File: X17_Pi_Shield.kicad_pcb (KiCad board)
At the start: 4 copper layers, 85 x 56 mm, 89 parts, among them J1 BM04B-GHS-TBT, J10 BM04B-GHS-TBT, J11 BM04B-GHS-TBT, J12 Conn_01x05_Pin, J13 Conn_01x03_Pin, J2 BM02B-GHS-TBT, J20 Conn_01x02_Pin, J22 430450212, J23 430450612, J24 430450212, J3 BM02B-GHS-TBT, J4 BM02B-GHS-TBT, J5 BM02B-GHS-TBT, J6 Conn_01x03_Pin, J7 BM04B-GHS-TBT, J8 UJC-HP-L-G-5-MSMT-TR, J9 Conn_01x03_Pin, U1 4754, U10 4754, U2 TPS2117DRLR, U3 INA260AIPW, U5 MAX485, U6 MMBT3906LT3G, U7 ISOW1432BDFMR, U8 RASPBERRY_PI_4B_4GB, U9 AZ1117IH-3.3TRG1

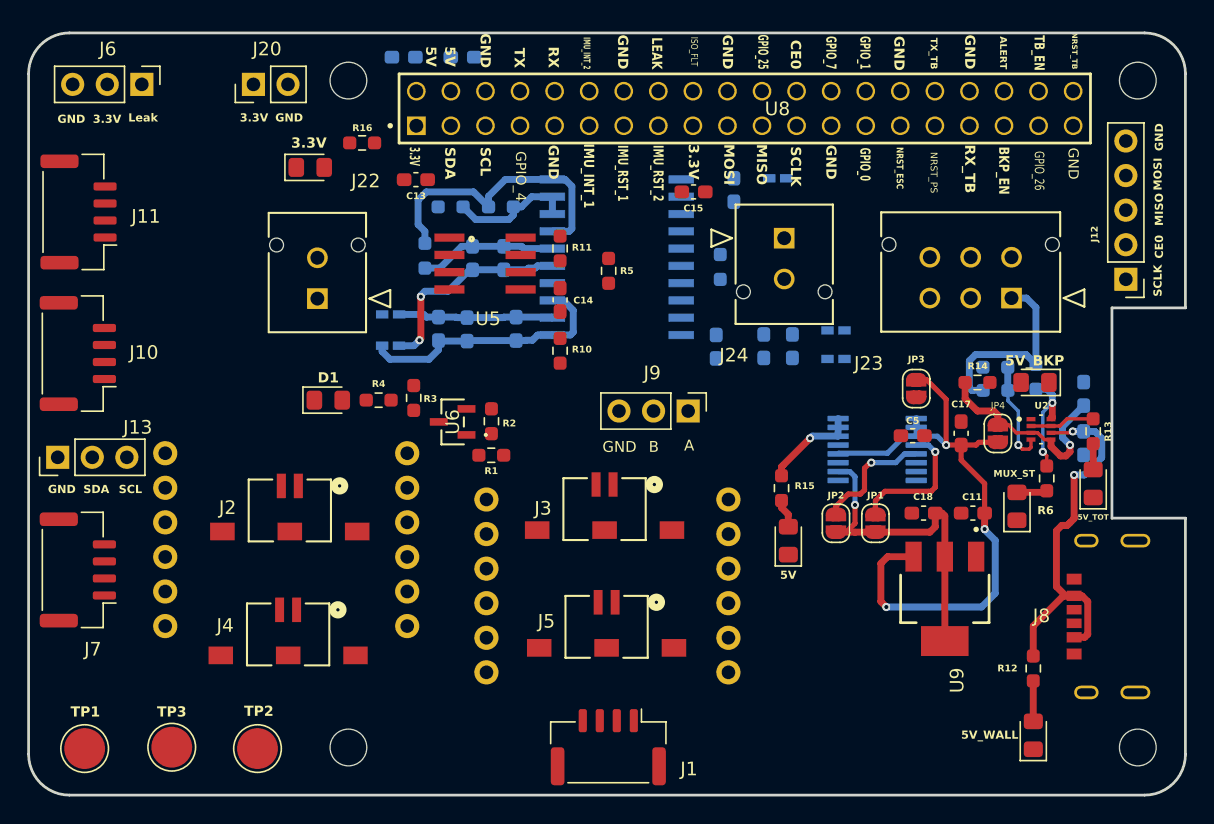
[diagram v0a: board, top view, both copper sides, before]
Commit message: Routing Additions
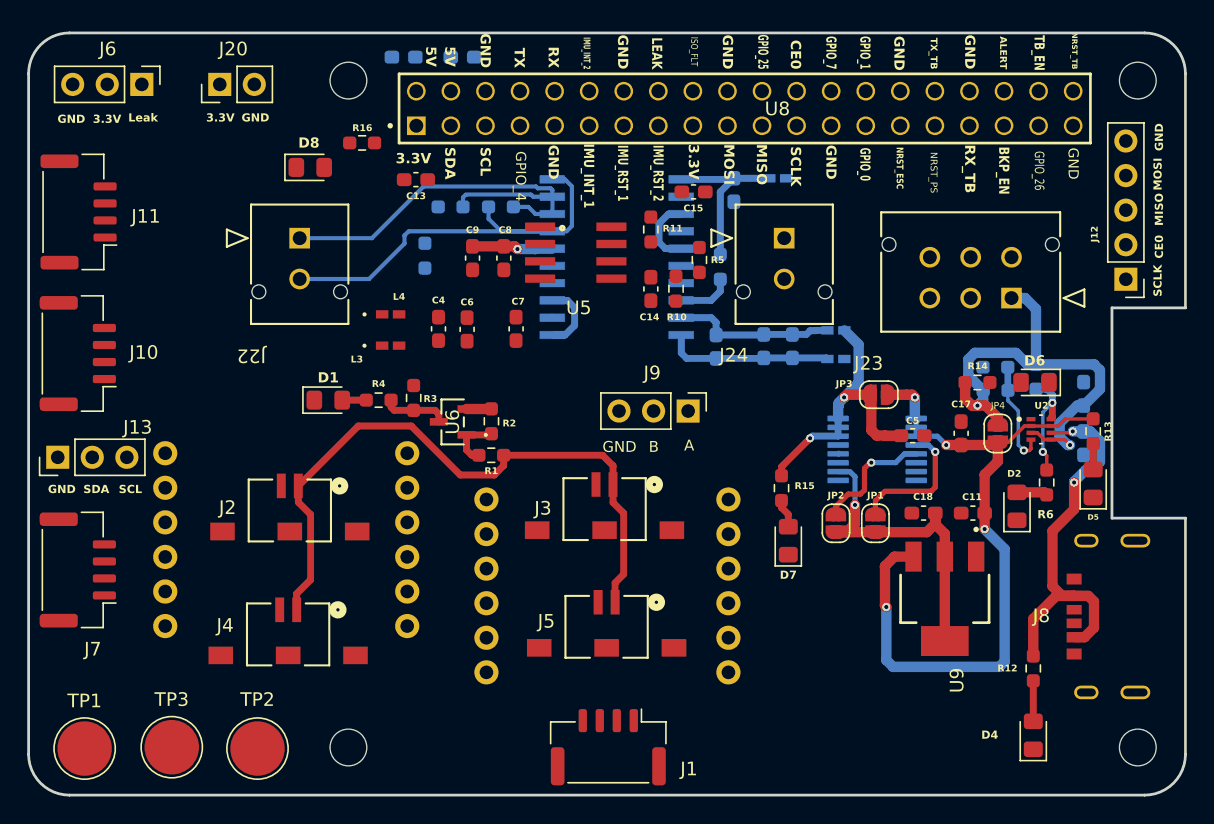
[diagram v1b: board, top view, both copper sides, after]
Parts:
- C4, C6, C7, C8, C9, L3, L4: moved to F.Cu
- TP1, TP2, TP3: footprint TestPoint:TestPoint_Pad_D3.0mm -> TestPoint:TestPoint_Pad_D4.0mm
- moved R10 9.66 mm to (157.2, 97.0)
- moved R11 6.81 mm to (155.4, 92.7)
- moved U5 6.72 mm to (149.9, 94.4)
- moved C14 6.72 mm to (155.4, 97.0)
- moved R5 6.72 mm to (159.0, 94.9)
- moved J22 4.63 mm to (129.6, 93.3), turned to 180 degrees
- moved JP3 2.79 mm to (172.2, 104.8), turned to 180 degrees
- moved J20 2.48 mm to (123.7, 82.0)
- moved R6 0.30 mm to (184.5, 111.2)
- renumbered MUX_ST to D2, 5V_WALL to D4, 5V_TOT to D5, 5V_BKP to D6, 5V to D7, 3.3V to D8
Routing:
- net /Sensors/PROBE: track 0.00 -> 48.3 mm
- net Net-(U7-B): track 9.26 -> 32.5 mm
- net GND_TB: track 15.6 -> 0.18 mm, vias 2 -> 0
- net +5V: track 7.04 -> 21.5 mm, vias 1 -> 2
- net Net-(U7-GND2): track 19.4 -> 5.09 mm
- net Net-(U7-VIO): track 0.00 -> 12.5 mm
- net Net-(U7-GND1): track 0.00 -> 12.3 mm
- net Net-(U7-VDD): track 0.00 -> 11.9 mm
- net Net-(U7-VISOOUT): track 11.4 -> 0.06 mm
- net Net-(U7-A): track 21.5 -> 32.5 mm
- net /Power/5V_BACKPLANE: track 30.4 -> 36.0 mm, vias 1 -> 2
- net /Pi + IMU/TB_EN: track 0.00 -> 5.13 mm
- net /Pi + IMU/LEAK: track 0.00 -> 4.81 mm
- net +3V3_TB: track 10.1 -> 5.95 mm, vias 0 -> 1
- net Net-(U6-BASE): track 0.00 -> 4.05 mm
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- added copper zone on In2.Cu, net +3V3
- added copper zone on In1.Cu, net GND

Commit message: Finished Routing
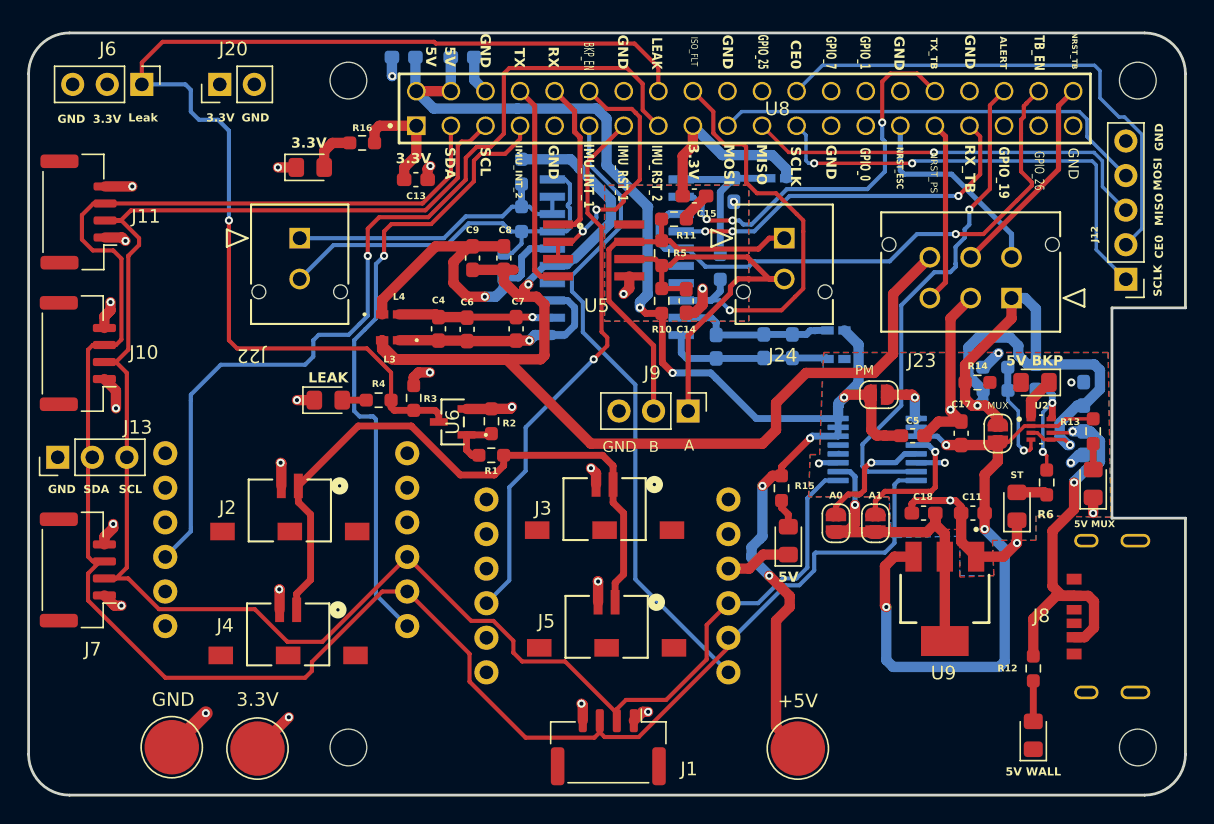
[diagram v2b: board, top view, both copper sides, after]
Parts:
- 5V BKP: renamed from D6
- 5V MUX: renamed from D5
- 5V WALL: renamed from D4
- moved +5V 52.4 mm to (166.2, 130.8)
- moved R20 5.85 mm to (144.6, 95.3)
- moved R19 5.82 mm to (145.9, 88.4), turned to 90 degrees
- moved R5 2.81 mm to (156.2, 94.4)
- moved C14 2.74 mm to (158.0, 97.9)
- moved R11 1.86 mm to (157.1, 91.9), turned to 0 degrees
- moved R17 1.76 mm to (145.9, 91.9), turned to -90 degrees
- moved R10 1.38 mm to (156.2, 97.9)
- moved U5 1.33 mm to (151.2, 94.2)
- moved L3 0.40 mm to (136.3, 100.8), turned to 180 degrees
- moved C15 0.31 mm to (158.6, 90.2)
- renumbered TP1 to +5V, D8 to 3.3V, TP2 to 3.3V, D7 to 5V, JP2 to A0, JP1 to A1, TP3 to GND, D1 to LEAK, JP4 to MUX, JP3 to PM, D2 to ST
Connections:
- U8 pad 07: (no net) -> /Pi + IMU/IMU_INT_2
- U8 pad 12: /Pi + IMU/IMU_INT_2 -> /Pi + IMU/BKP_EN
- U8 pad 35: /Pi + IMU/BKP_EN -> unconnected-(U8-GPIO19-Pad35)
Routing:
- net /Pi + IMU/SDA: track 0.00 -> 151.1 mm
- net /Pi + IMU/SCL: track 0.00 -> 139.9 mm
- net GND_TB: track 0.18 -> 96.1 mm, vias 0 -> 1
- net /Pi + IMU/LEAK: track 4.81 -> 86.6 mm, vias 0 -> 1
- net +5V: track 21.5 -> 102.9 mm, vias 2 -> 6
- net GND: track 0.00 -> 75.6 mm, vias 0 -> 26
- net /Pi + IMU/IMU_RST_2: track 0.00 -> 67.9 mm, vias 0 -> 1
- net /Pi + IMU/IMU_INT_1: track 0.00 -> 47.4 mm
- net /Pi + IMU/IMU_INT_2: track 0.00 -> 46.8 mm, vias 0 -> 1
- net /Pi + IMU/IMU_RST_1: track 0.00 -> 40.5 mm, vias 0 -> 1
- net /Pi + IMU/CE0: track 0.00 -> 38.0 mm
- net /Pi + IMU/ALERT: track 0.00 -> 36.7 mm, vias 0 -> 1
- net /Pi + IMU/TB_EN: track 5.13 -> 41.7 mm, vias 0 -> 1
- net +3V3: track 1.84 -> 36.4 mm, vias 0 -> 6
- net /Pi + IMU/SCLK: track 0.00 -> 33.8 mm, vias 0 -> 2
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- added copper zone on B.Cu, net GND
- added copper zone on F.Cu, net GND
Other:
- board text added: "GPIO_19"
- board text removed: "GPIO_4"

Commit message: Finished Layout + Updated Capacitor Sizes for 150uF
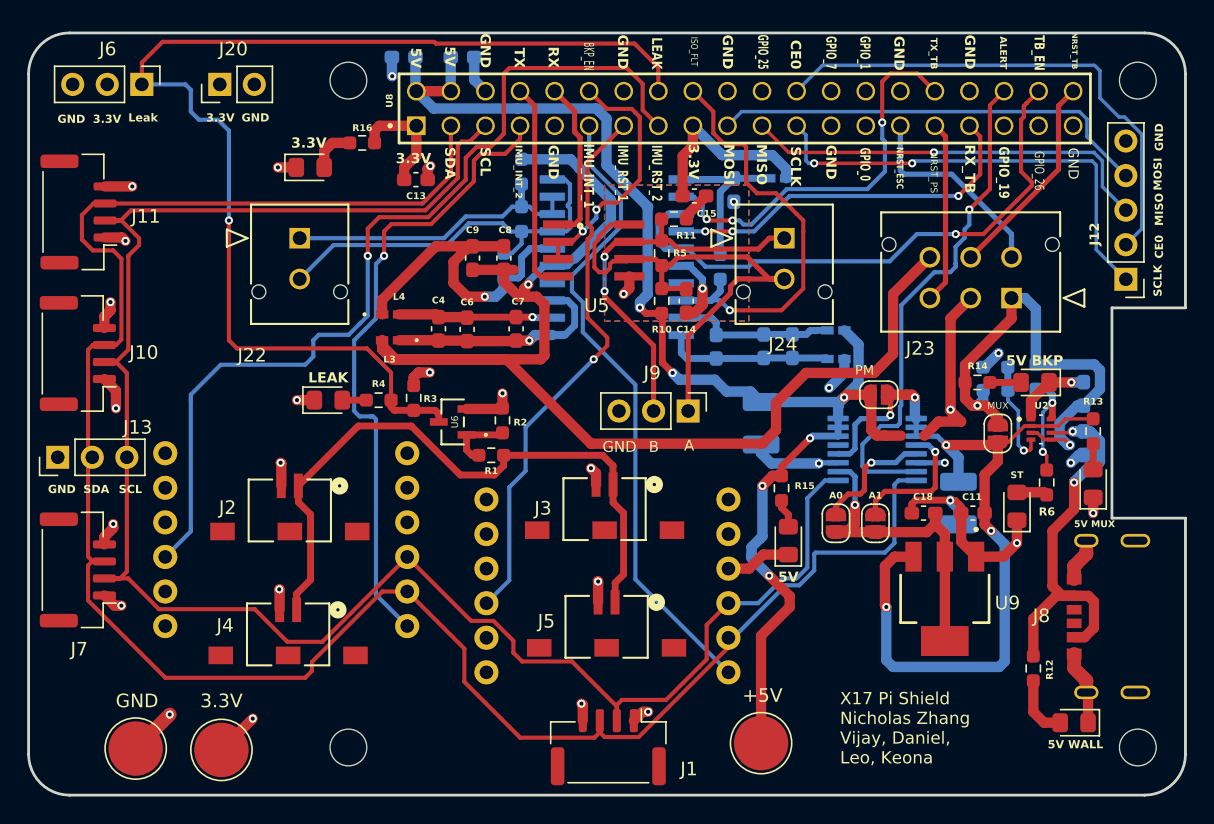
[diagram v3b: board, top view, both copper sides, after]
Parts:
- C17, C5: footprint Capacitor_SMD:C_0603_1608Metric_Pad1.08x0.95mm_HandSolder -> Capacitor_SMD:C_1210_3225Metric_Pad1.33x2.70mm_HandSolder; moved to B.Cu
- moved C5 11.2 mm to (163.5, 106.9), turned to -90 degrees
- moved C17 5.13 mm to (178.0, 112.8), turned to -90 degrees
- moved 5V WALL 3.14 mm to (186.5, 128.9), turned to 180 degrees
- moved +5V 2.73 mm to (163.5, 130.4)
- moved GND 2.65 mm to (117.5, 130.8)
- moved 3.3V 2.65 mm to (123.8, 130.9)
- moved R2 0.81 mm to (144.5, 106.7)
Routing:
- net GND: track 75.6 -> 99.3 mm, vias 26 -> 27
- net /Power/5V_TOTAL: track 54.7 -> 65.3 mm, vias 4 -> 5
- net /Power/5V_BACKPLANE: track 45.5 -> 35.4 mm
- net /UART/A: track 30.7 -> 39.0 mm
- net Net-(D6-A): track 0.00 -> 2.29 mm
- net Net-(D4-A): track 2.98 -> 4.58 mm
- net Net-(U6-BASE): track 4.05 -> 4.88 mm
- net /Pi + IMU/ALERT: track 36.7 -> 37.4 mm
- net /Pi + IMU/SCL: track 139.9 -> 140.5 mm
- net /Pi + IMU/SDA: track 151.1 -> 151.7 mm
- net +5V: track 102.9 -> 102.4 mm
- net /UART/B: track 28.8 -> 29.1 mm, vias 0 -> 2
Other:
- board text added: "X17 Pi Shield Nicholas Zhang Vijay, Daniel, Leo, Keona"

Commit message: Tweaking 150uF
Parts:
- moved C17 1.26 mm to (179.0, 112.0)
- moved R15 0.52 mm to (165.5, 111.8)
- moved C5 0.51 mm to (164.0, 106.8)
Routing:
- net GND: track 99.3 -> 87.4 mm, vias 27 -> 26
- net +5V: track 102.4 -> 98.8 mm
- net /Power/5V_TOTAL: track 65.3 -> 66.5 mm

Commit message: Silkscreen
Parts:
- added G***: LOGO, Custom Guitar Graphic:john, F.Cu at (168.6, 124.1)
- added G***: LOGO, Custom Guitar Graphic:diff_2_guitar_1, F.Cu at (174.6, 129.1)
- moved C14 9.29 mm to (153.8, 89.6), turned to -90 degrees
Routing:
- net /Power/5V_TOTAL: track 66.5 -> 53.6 mm
- net /Pi + IMU/BKP_EN: track 18.6 -> 9.93 mm
- net GND: track 87.4 -> 84.8 mm
- net GND_TB: track 96.3 -> 95.6 mm
- net /UART/A: track 39.0 -> 39.6 mm
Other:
- board text added: "John Mayer"
- board text added: "X17 Pi Shield Nicholas Zhang Vijay, Daniel Leo, Keona"
- board text removed: "X17 Pi Shield Nicholas Zhang Vijay, Daniel, Leo, Keona"

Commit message: MAX 485
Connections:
- C14 pad 2: /UART/A -> +5V
- U5 pad 8: /UART/A -> +5V
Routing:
- net /UART/A: track 39.6 -> 29.9 mm
- net +5V: track 98.3 -> 100.1 mm
- net GND: track 84.8 -> 86.4 mm, vias 26 -> 27
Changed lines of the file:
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@@
 		(tags "capacitor handsolder")
 		(property "Reference" "C14"
-			(at -2.0875 0 360)
+			(at -2.0875 0 0)
 			(layer "F.SilkS")
 			(effects
@@
 			(layers "F.Cu" "F.Paste" "F.Mask")
 			(roundrect_rratio 0.25)
-			(net 71 "/UART/A")
+			(net 6 "+5V")
 			(pintype "passive")
 		)
@@
 			(size 0.6096 2.2098)
 			(layers "F.Cu" "F.Paste" "F.Mask")
-			(net 71 "/UART/A")
+			(net 6 "+5V")
 			(pinfunction "VCC")
 			(pintype "bidirectional")
@@
 			(pts
 				(xy -2.151472 3.613806) (xy -2.109957 3.638348) (xy -2.07826 3.678352) (xy -2.060963 3.730328) (xy -2.063062 3.77925)
-				(xy -2.082912 3.822126) (xy -2.116037 3.855987) (xy -2.157959 3.877868) (xy -2.2042 3.884803) (xy -2.250285 3.873824)
+				(xy -2.082912 3.822126) (xy -2.116037 3.855987) (xy -2.157959 3.877867) (xy -2.2042 3.884803) (xy -2.250285 3.873824)
 				(xy -2.265033 3.865543) (xy -2.308379 3.825904) (xy -2.332061 3.779453) (xy -2.3356 3.730017) (xy -2.318519 3.68142)
 				(xy -2.292211 3.64814) (xy -2.246871 3.617184) (xy -2.198534 3.606245)
@@
 			(pts
 				(xy 3.592055 -4.65855) (xy 3.618289 -4.626342) (xy 3.632516 -4.578316) (xy 3.634677 -4.55921) (xy 3.631263 -4.545136)
-				(xy 3.618537 -4.53211) (xy 3.592763 -4.516146) (xy 3.555285 -4.495954) (xy 3.511004 -4.472179) (xy 3.469886 -4.449603)
+				(xy 3.618537 -4.53211) (xy 3.592763 -4.516146) (xy 3.555285 -4.495954) (xy 3.511004 -4.47218) (xy 3.469886 -4.449603)
 				(xy 3.439717 -4.432513) (xy 3.436052 -4.430351) (xy 3.400202 -4.408973) (xy 3.376388 -4.447505)
 				(xy 3.35489 -4.496264) (xy 3.354458 -4.540257) (xy 3.375569 -4.580762) (xy 3.418702 -4.61906) (xy 3.447137 -4.636902)
@@
 				(xy 5.408695 -4.733722) (xy 5.382384 -4.654582) (xy 5.337286 -4.581381) (xy 5.27384 -4.517055) (xy 5.233423 -4.487886)
 				(xy 5.174104 -4.455525) (xy 5.116486 -4.437462) (xy 5.054572 -4.432945) (xy 4.982366 -4.441224)
-				(xy 4.937022 -4.450741) (xy 4.89347 -4.459725) (xy 4.854795 -4.463994) (xy 4.819482 -4.46215) (xy 4.786013 -4.452782)
+				(xy 4.937022 -4.450741) (xy 4.89347 -4.459725) (xy 4.854795 -4.463994) (xy 4.819482 -4.462151) (xy 4.786013 -4.452782)
 				(xy 4.752874 -4.434492) (xy 4.718548 -4.405875) (xy 4.68152 -4.365528) (xy 4.640274 -4.312047) (xy 4.593293 -4.244028)
 				(xy 4.539063 -4.160069) (xy 4.476066 -4.058766) (xy 4.427042 -3.978589) (xy 4.35775 -3.866163) (xy 4.297938 -3.772202)
@@
 				(xy -0.5157 1.87447) (xy -0.539356 1.870946) (xy -0.545502 1.87004) (xy -0.569033 1.862414) (xy -0.605005 1.846098)
 				(xy -0.646591 1.824453) (xy -0.686958 1.800839) (xy -0.68987 1.799005) (xy -0.7322 1.769752) (xy -0.773419 1.735695)
-				(xy -0.815599 1.694478) (xy -0.860812 1.643747) (xy -0.911129 1.581146) (xy -0.968625 1.50432) (xy -1.035368 1.410914)
+				(xy -0.815599 1.694478) (xy -0.860812 1.643747) (xy -0.911129 1.581146) (xy -0.968626 1.50432) (xy -1.035368 1.410914)
 				(xy -1.05123 1.38829) (xy -1.079291 1.350625) (xy -1.104944 1.320521) (xy -1.12394 1.302814) (xy -1.128397 1.300385)
 				(xy -1.152329 1.304328) (xy -1.186735 1.328243) (xy -1.193957 1.3346) (xy -1.219556 1.35487) (xy -1.244119 1.366383)
@@
 	)
 	(segment
+		(start 153.85 88.35)
+		(end 154.7 87.5)
+		(width 0.762)
+		(layer "F.Cu")
+		(net 5)
+	)
+	(segment
 		(start 128.25 109.85)
 		(end 128.2 109.8)
@@
 	)
 	(segment
+		(start 153.85 88.7375)
+		(end 153.85 88.35)
+		(width 0.762)
+		(layer "F.Cu")
+		(net 5)
+	)
+	(segment
 		(start 186.5 123.85)
 		(end 186.5 124.9)
@@
 	)
 	(via
+		(at 154.7 87.5)
+		(size 0.6)
+		(drill 0.3)
+		(layers "F.Cu" "B.Cu")
+		(net 5)
+	)
+	(via
 		(at 182.3 115.7)
 		(size 0.6)
@@
 	)
 	(segment
+		(start 153.8162 90.4963)
+		(end 153.85 90.4625)
+		(width 0.762)
+		(layer "F.Cu")
+		(net 6)
+	)
+	(segment
 		(start 138.17 82.5)
 		(end 140.71 82.5)
@@
 	)
 	(segment
+		(start 153.8162 92.295)
+		(end 153.8162 90.4963)
+		(width 0.762)
+		(layer "F.Cu")
+		(net 6)
+	)
+	(segment
 		(start 156.2 98.825)
 		(end 155.025 98.825)
@@
 	)
 	(segment
-		(start 153.85 90.4625)
-		(end 153.85 92.2612)
-		(width 0.762)
-		(layer "F.Cu")
-		(net 71)
-	)
-	(segment
-		(start 151.715047 95.356921)
-		(end 151.310562 94.952436)
-		(width 0.381)
-		(layer "F.Cu")
-		(net 71)
-	)
-	(segment
 		(start 162.60421 96.3)
 		(end 162.593711 96.289501)
@@
 	)
 	(segment
-		(start 152.865 94.835)
-		(end 152.343079 95.356921)
-		(width 0.381)
-		(layer "F.Cu")
-		(net 71)
-	)
-	(segment
-		(start 151.6 93.978342)
-		(end 151.6 92)
-		(width 0.381)
-		(layer "F.Cu")
-		(net 71)
-	)
-	(segment
 		(start 157.7 94.7)
 		(end 157.719 94.681)
@@
 	)
 	(segment
-		(start 151.310562 94.26778)
-		(end 151.6 93.978342)
-		(width 0.381)
-		(layer "F.Cu")
-		(net 71)
-	)
-	(segment
 		(start 156.7875 95.3125)
 		(end 157.4 94.7)
@@
 	)
 	(segment
-		(start 151.6 92)
-		(end 153.1375 90.4625)
-		(width 0.381)
-		(layer "F.Cu")
-		(net 71)
-	)
-	(segment
-		(start 153.85 92.2612)
-		(end 153.8162 92.295)
-		(width 0.762)
-		(layer "F.Cu")
-		(net 71)
-	)
-	(segment
 		(start 155.7225 94.835)
 		(end 156.2 95.3125)
@@
 	)
 	(segment
-		(start 151.310562 94.952436)
-		(end 151.310562 94.26778)
-		(width 0.381)
-		(layer "F.Cu")
-		(net 71)
-	)
-	(segment
-		(start 152.343079 95.356921)
-		(end 151.715047 95.356921)
-		(width 0.381)
-		(layer "F.Cu")
-		(net 71)
-	)
-	(segment
 		(start 161.806291 96.289501)
 		(end 161.249501 96.846291)
@@
 		(width 0.381)
 		(layer "F.Cu")
-		(net 71)
-	)
-	(segment
-		(start 153.1375 90.4625)
-		(end 153.85 90.4625)
-		(width 0.381)
-		(layer "F.Cu")

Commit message: Last Updates + Adding Screenshots
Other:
- board text added: "-JM"
- board text removed: "John Mayer"
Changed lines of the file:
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@@
 	)
 	(gr_text "X17 Pi Shield\nNicholas Zhang\nVijay, Daniel\nLeo, Keona"
-		(at 179.3 128.6 0)
+		(at 179.3 128.5 0)
 		(layer "B.SilkS")
 		(effects
@@
 		)
 	)
-	(gr_text "John Mayer\n"
-		(at 166.5 119.8 0)
-		(layer "F.SilkS")
-		(effects
+	(gr_text "-JM"
+		(at 176.7 130.3 0)
+		(layer "F.SilkS")
+		(effects
